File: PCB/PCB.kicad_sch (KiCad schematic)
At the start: 6 parts

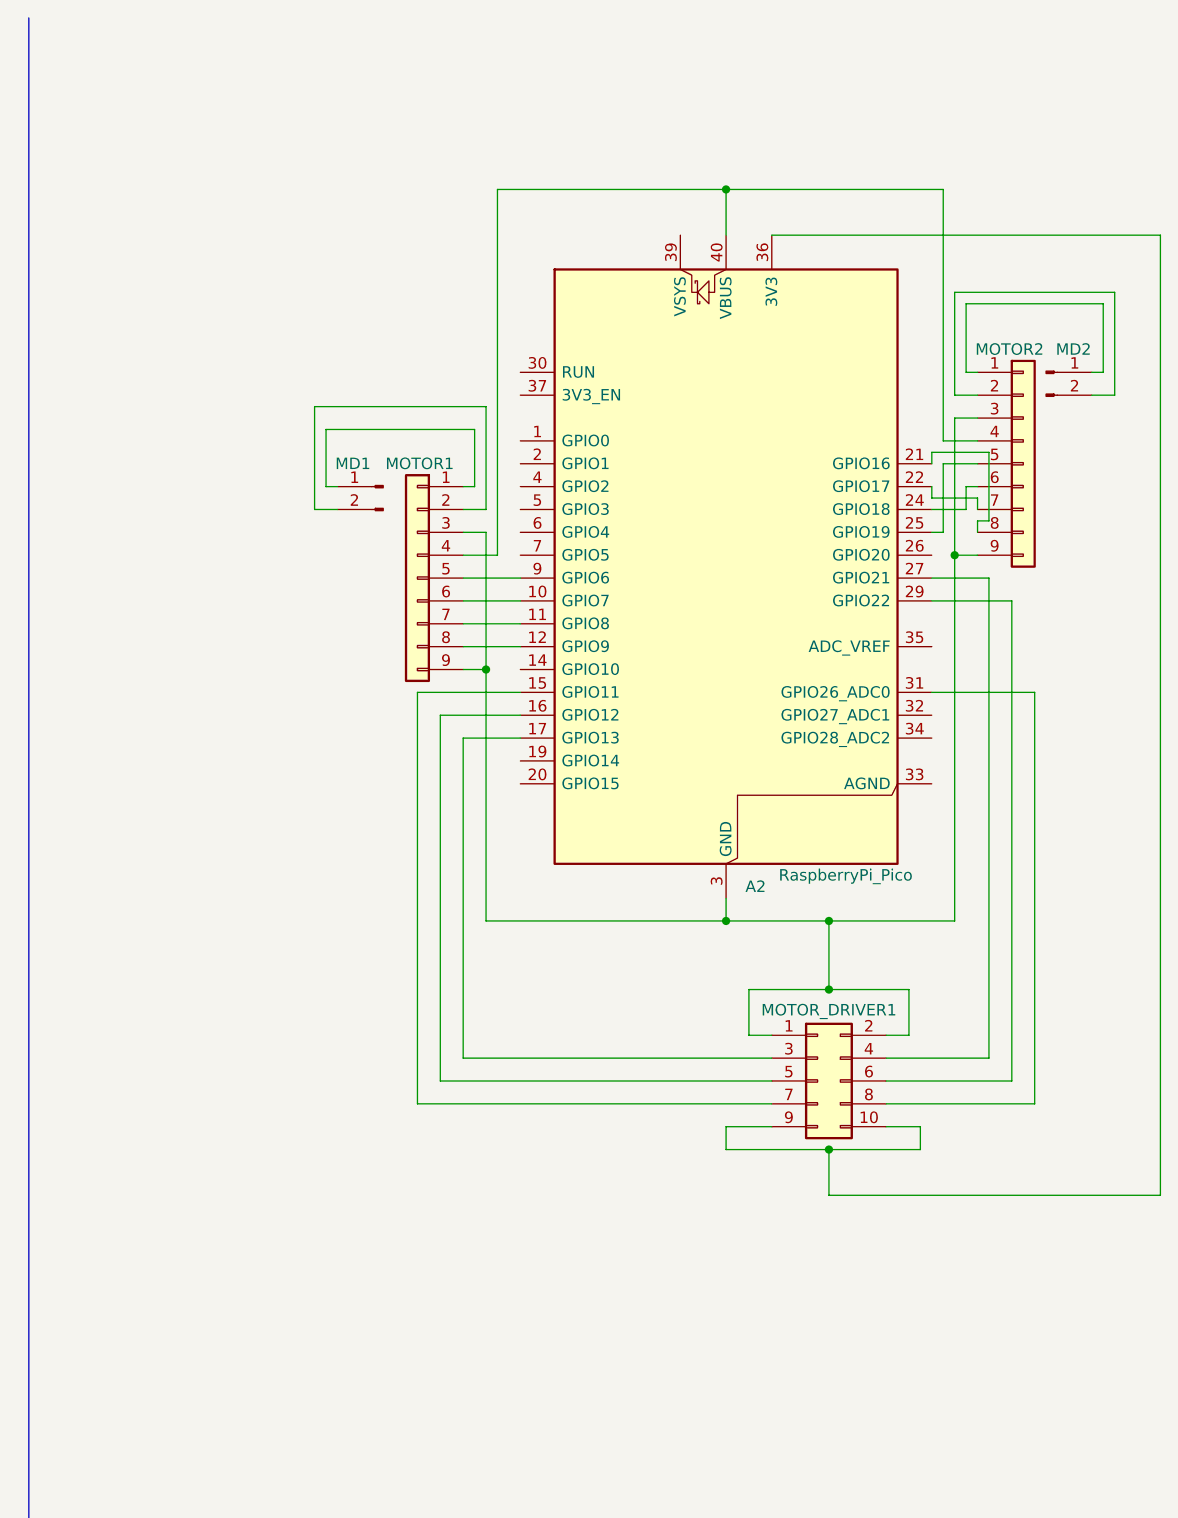
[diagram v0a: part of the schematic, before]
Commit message: update motor driver connection
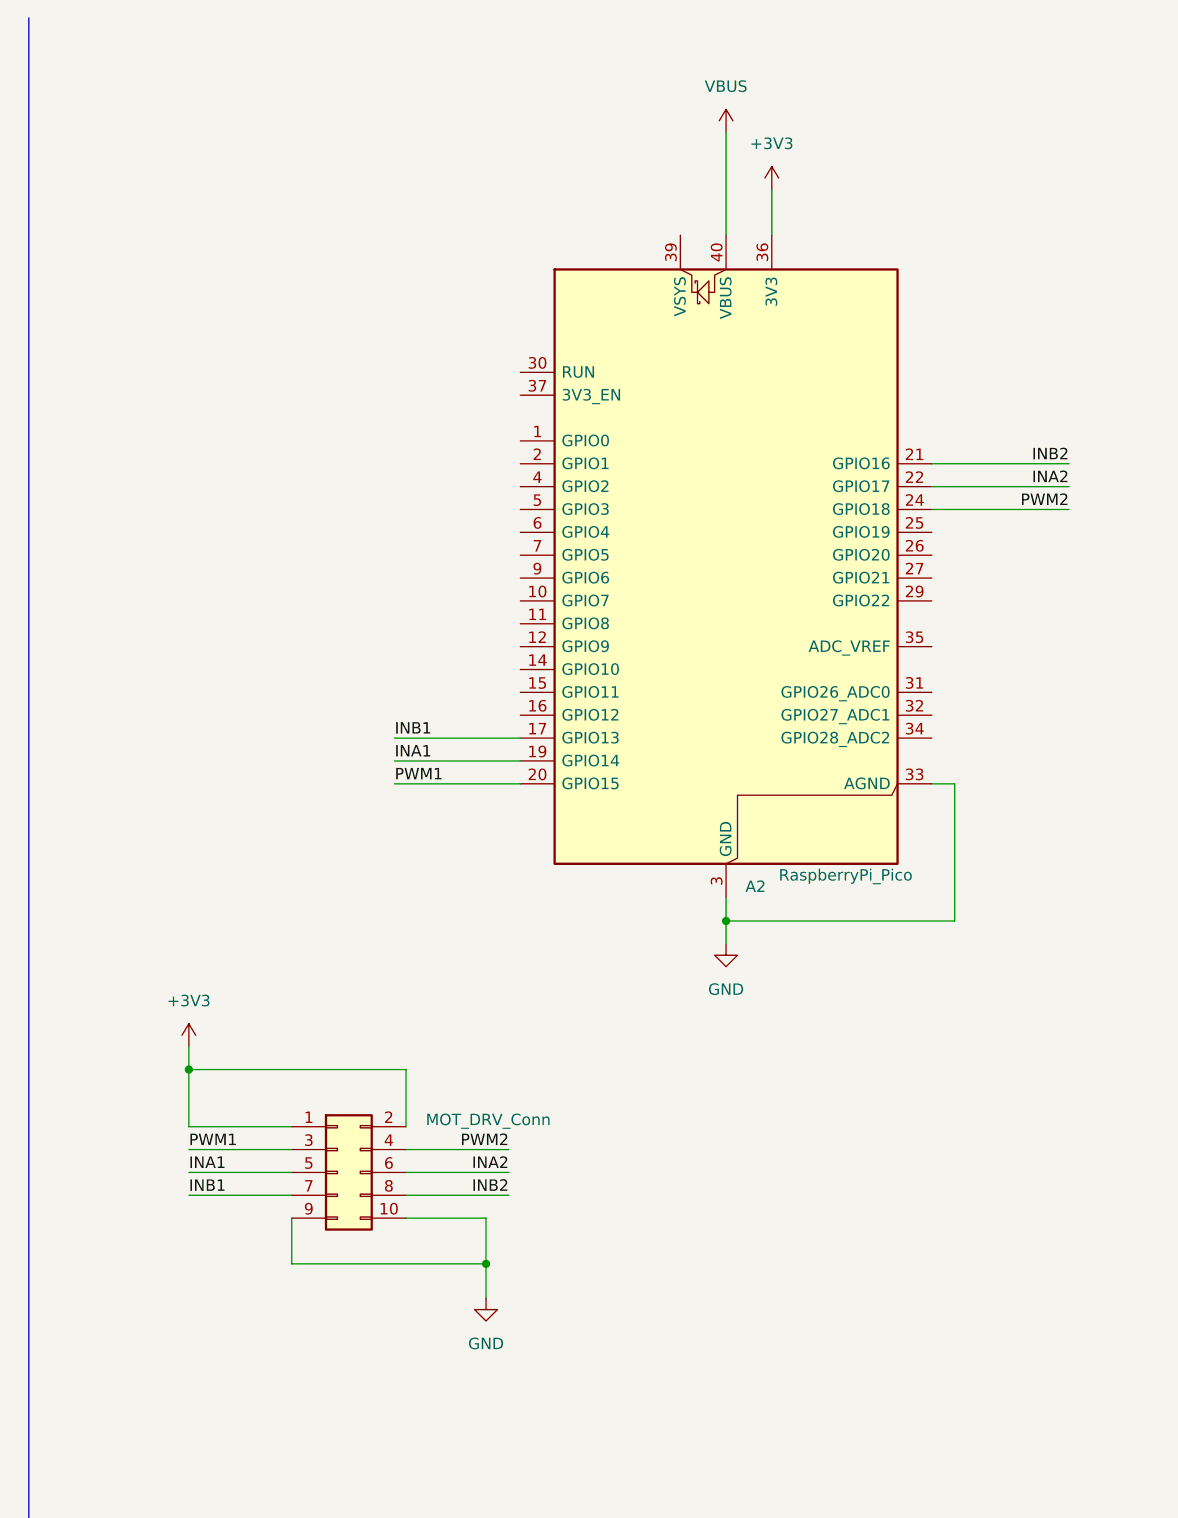
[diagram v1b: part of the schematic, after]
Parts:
- removed MD1, MD2: Conn_01x02_Pin, Connector_PinHeader_2.54mm:PinHeader_1x02_P2.54mm_Vertical, symbol Connector:Conn_01x02_Pin
- removed MOTOR1, MOTOR2: Conn_01x09, Connector_PinHeader_2.54mm:PinHeader_1x09_P2.54mm_Vertical, symbol Connector_Generic:Conn_01x09
- renumbered MOTOR_DRIVER1 to MOT_DRV_Conn
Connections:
- net GND: now reaches A2.13 (GND), A2.18 (GND), A2.23 (GND), A2.28 (GND), A2.3 (GND), A2.38 (GND), A2.8 (GND)
- net GND: now also A2.33 (AGND), MOT_DRV_Conn.10 (Pin_10), MOT_DRV_Conn.9 (Pin_9); no longer MOT_DRV_Conn.1 (Pin_1), MOT_DRV_Conn.2 (Pin_2)
- net VBUS: now reaches A2.40 (VBUS)
- net PWM2: now reaches A2.24 (GPIO18)
- net PWM2: now also MOT_DRV_Conn.4 (Pin_4)
- net INA2: now reaches A2.22 (GPIO17)
- net INA2: now also MOT_DRV_Conn.6 (Pin_6)
- net INB2: now reaches A2.21 (GPIO16)
- net INB2: now also MOT_DRV_Conn.8 (Pin_8)
- net INB1: now reaches A2.17 (GPIO13)
- net INB1: now also MOT_DRV_Conn.7 (Pin_7); no longer MOT_DRV_Conn.3 (Pin_3)
- net at A2.27 (GPIO21): no longer MOT_DRV_Conn.4 (Pin_4)
- net at A2.16 (GPIO12): no longer MOT_DRV_Conn.5 (Pin_5)
- net at A2.29 (GPIO22): no longer MOT_DRV_Conn.6 (Pin_6)
- net at A2.15 (GPIO11): no longer MOT_DRV_Conn.7 (Pin_7)
- net at A2.31 (GPIO26_ADC0): no longer MOT_DRV_Conn.8 (Pin_8)
- net INA1: now reaches A2.19 (GPIO14)
- net INA1: now also MOT_DRV_Conn.5 (Pin_5)
- net PWM1: now reaches A2.20 (GPIO15)
- net PWM1: now also MOT_DRV_Conn.3 (Pin_3)
- new net +3V3: A2.36 (3V3), MOT_DRV_Conn.1 (Pin_1), MOT_DRV_Conn.2 (Pin_2)
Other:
- moved on the sheet: MOT_DRV_Conn

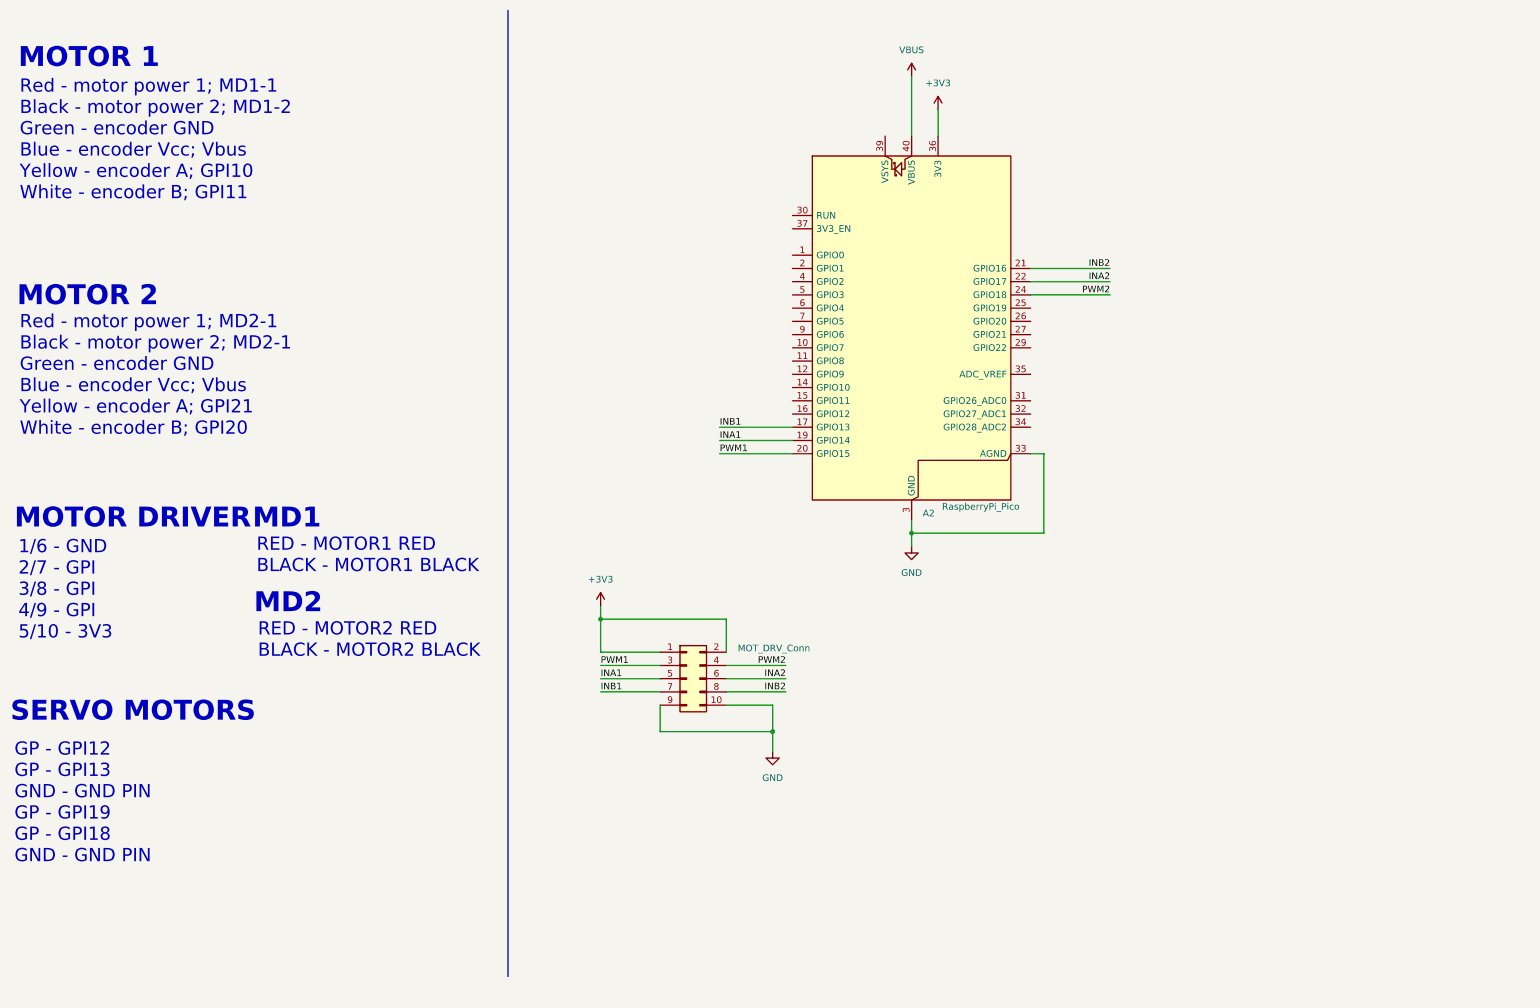
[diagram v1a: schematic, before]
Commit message: update sch with new motor driver connections and servos
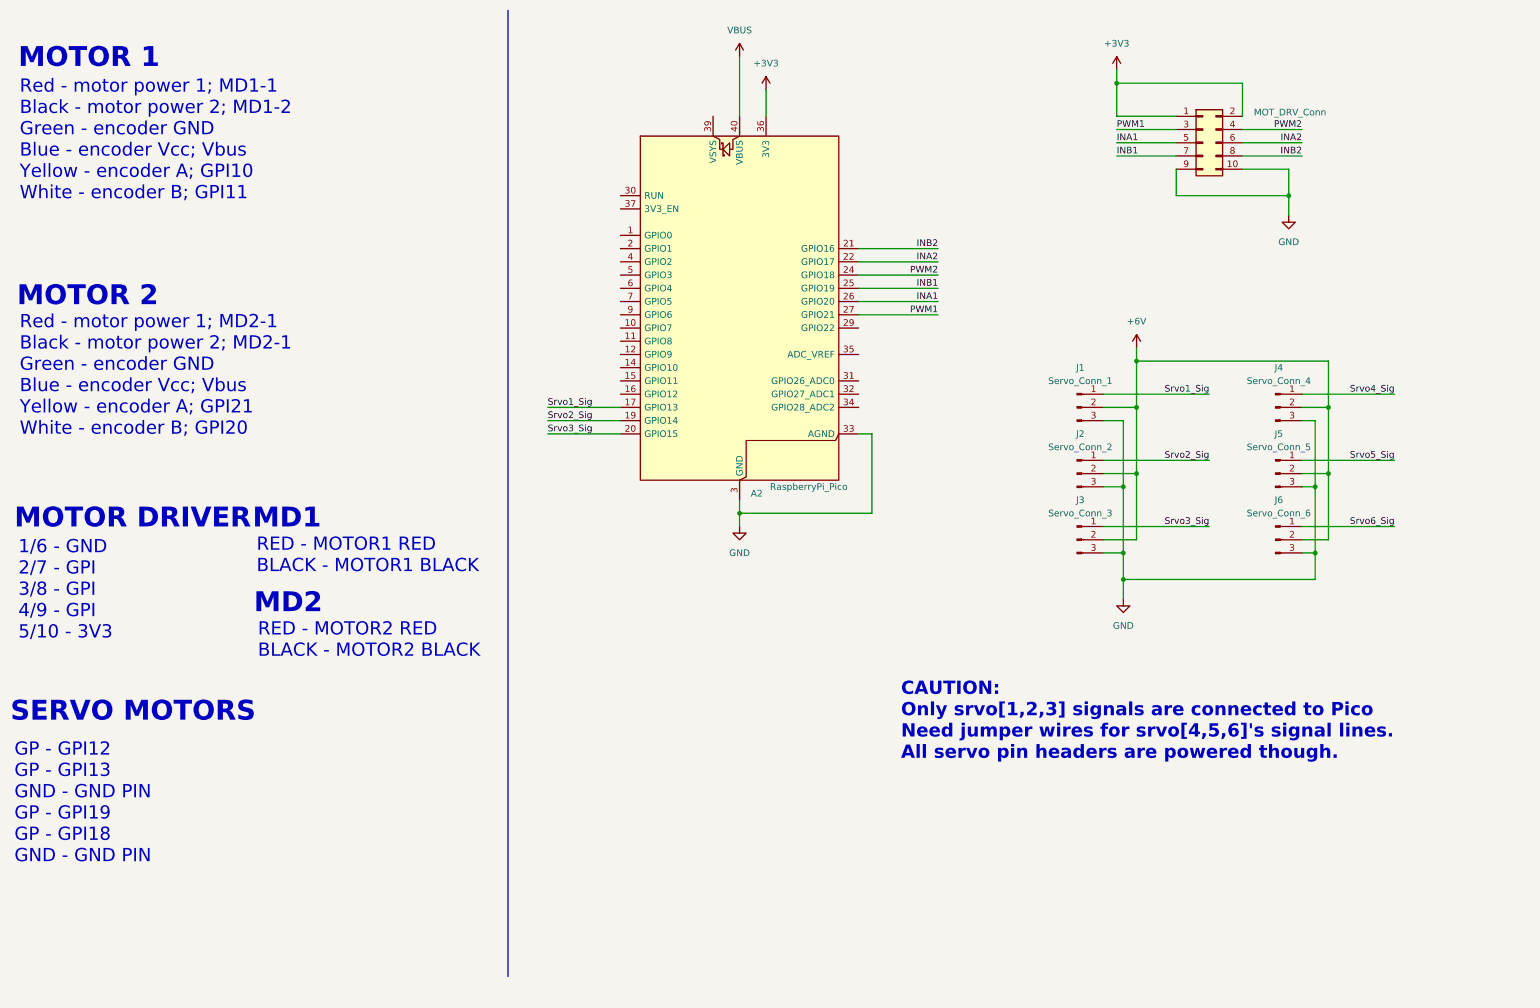
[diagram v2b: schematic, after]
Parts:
- added J1: Servo_Conn_1, symbol Connector:Conn_01x03_Pin
- added J2: Servo_Conn_2, symbol Connector:Conn_01x03_Pin
- added J3: Servo_Conn_3, symbol Connector:Conn_01x03_Pin
- added J4: Servo_Conn_4, symbol Connector:Conn_01x03_Pin
- added J5: Servo_Conn_5, symbol Connector:Conn_01x03_Pin
- added J6: Servo_Conn_6, symbol Connector:Conn_01x03_Pin
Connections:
- net GND: now also J1.3 (Pin_3), J2.3 (Pin_3), J3.3 (Pin_3), J4.3 (Pin_3), J5.3 (Pin_3), J6.3 (Pin_3)
- net INA1: now also A2.26 (GPIO20); no longer A2.19 (GPIO14)
- net INB1: now also A2.25 (GPIO19); no longer A2.17 (GPIO13)
- net PWM1: now also A2.27 (GPIO21); no longer A2.20 (GPIO15)
- new net +6V: J1.2 (Pin_2), J2.2 (Pin_2), J3.2 (Pin_2), J4.2 (Pin_2), J5.2 (Pin_2), J6.2 (Pin_2)
- new net Srvo1_Sig: A2.17 (GPIO13), J1.1 (Pin_1)
- new net Srvo2_Sig: A2.19 (GPIO14), J2.1 (Pin_1)
- new net Srvo3_Sig: A2.20 (GPIO15), J3.1 (Pin_1)
- new net Srvo4_Sig: J4.1 (Pin_1)
- new net Srvo5_Sig: J5.1 (Pin_1)
- new net Srvo6_Sig: J6.1 (Pin_1)
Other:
- note added: "CAUTION: Only srvo[1,2,3] signals are connected to Pico Need jumper wires for srvo[4,5,6]'s signal lines. All servo pin headers are powered though."
- moved on the sheet: A2, MOT_DRV_Conn

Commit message: modify micha's notes
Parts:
- added D1: LED_RKGB, symbol Device:LED_RKGB
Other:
- note removed: "1/6 - GND 2/7 - GPI 3/8 - GPI 4/9 - GPI 5/10 - 3V3"
- note removed: "GP - GPI12 GP - GPI13 GND - GND PIN GP - GPI19 GP - GPI18 GND - GND PIN"
- note removed: "MOTOR DRIVER"
- note removed: "SERVO MOTORS"
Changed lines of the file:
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@@
 	(text "MD1"
 		(exclude_from_sim no)
-		(at 61.468 110.236 0)
+		(at 18.288 96.52 0)
 		(effects
 			(font
 				(face "KiCad Font")
-				(size 3.81 3.81)
+				(size 2.54 2.54)
 				(thickness 0.762)
 				(bold yes)
@@
 	(text "RED - MOTOR1 RED\nBLACK - MOTOR1 BLACK"
 		(exclude_from_sim no)
-		(at 62.23 117.348 0)
+		(at 19.05 103.632 0)
 		(effects
 			(font
 				(face "KiCad Font")
-				(size 2.54 2.54)
+				(size 1.27 1.27)
 			)
 			(justify left)
@@
 	(text "RED - MOTOR2 RED\nBLACK - MOTOR2 BLACK"
 		(exclude_from_sim no)
-		(at 62.484 133.604 0)
+		(at 19.304 119.888 0)
 		(effects
 			(font
 				(face "KiCad Font")
-				(size 2.54 2.54)
+				(size 1.27 1.27)
 			)
 			(justify left)
@@
 			(font
 				(face "KiCad Font")
-				(size 3.81 3.81)
+				(size 2.54 2.54)
 				(thickness 0.762)
 				(bold yes)
@@
 			(font
 				(face "KiCad Font")
-				(size 2.54 2.54)
+				(size 1.27 1.27)
 			)
 			(justify left)
 		)
 	)
-	(text "GP - GPI12\nGP - GPI13\nGND - GND PIN\nGP - GPI19\nGP - GPI18\nGND - GND PIN"
+	(text "MD2"
 		(exclude_from_sim no)
-		(at 15.748 164.846 0)
+		(at 18.542 112.776 0)
 		(effects
 			(font
 				(face "KiCad Font")
 				(size 2.54 2.54)
-			)
-			(justify left)
-		)
-	)
-	(text "SERVO MOTORS"
-		(exclude_from_sim no)
-		(at 14.986 147.32 0)
-		(effects
-			(font
-				(face "KiCad Font")
-				(size 3.81 3.81)
-				(thickness 0.762)
-				(bold yes)
-			)
-			(justify left)
-		)
-	)
-	(text "MD2"
-		(exclude_from_sim no)
-		(at 61.722 126.492 0)
-		(effects
-			(font
-				(face "KiCad Font")
-				(size 3.81 3.81)
-				(thickness 0.762)
-				(bold yes)
-			)
-			(justify left)
-		)
-	)
-	(text "MOTOR DRIVER"
-		(exclude_from_sim no)
-		(at 15.748 110.236 0)
-		(effects
-			(font
-				(face "KiCad Font")
-				(size 3.81 3.81)
 				(thickness 0.762)
 				(bold yes)
@@
 			(font
 				(face "KiCad Font")
-				(size 3.81 3.81)
+				(size 2.54 2.54)
 				(thickness 0.762)
 				(bold yes)
-			)
-			(justify left)
-		)
-	)
-	(text "1/6 - GND\n2/7 - GPI\n3/8 - GPI\n4/9 - GPI\n5/10 - 3V3\n"
-		(exclude_from_sim no)
-		(at 16.51 123.952 0)
-		(effects
-			(font
-				(face "KiCad Font")
-				(size 2.54 2.54)
 			)
 			(justify left)
@@
 			(font
 				(face "KiCad Font")
-				(size 2.54 2.54)
+				(size 1.27 1.27)
 			)
 			(justify left)
@@
 			(width 0)
 			(type default)
-		)
-	)
-	(polyline
-		(pts
-			(xy 110.49 12.7) (xy 110.49 198.12)
-		)
-		(stroke
-			(width 0)
-			(type default)
-			(color 132 0 0 1)
 		)
 	)
@@
 					(unit 1)
 				)
+			)
+		)
+	)
+	(symbol
+		(lib_id "Device:LED_RKGB")
+		(at 135.89 162.56 0)
+		(unit 1)
+		(exclude_from_sim no)
+		(in_bom yes)
+		(on_board yes)
+		(dnp no)
+		(fields_autoplaced yes)
+		(property "Reference" "D1"
+			(at 135.89 148.59 0)
+			(effects
+				(font
+					(size 1.27 1.27)
+				)
+			)
+		)
+		(property "Value" "LED_RKGB"
+			(at 135.89 151.13 0)
+			(effects
+				(font
+					(size 1.27 1.27)
+				)
+			)
+		)
+		(property "Footprint" ""
+			(at 135.89 163.83 0)
+			(effects
+				(font
+					(size 1.27 1.27)
+				)
+				(hide yes)
+			)
+		)
+		(property "Datasheet" "~"
+			(at 135.89 163.83 0)
+			(effects
+				(font
+					(size 1.27 1.27)
+				)
+				(hide yes)
+			)
+		)
+		(property "Description" "RGB LED, red/cathode/green/blue"
+			(at 135.89 162.56 0)
+			(effects
+				(font
+					(size 1.27 1.27)
+				)
+				(hide yes)
+			)
+		)
+		(pin "1"
+		)
+		(pin "4"
+		)
+		(pin "3"
+		)
+		(pin "2"
+		)
+		(instances
+			(project ""
+				(path "/108ca819-7acb-4683-8ce1-30bbf8b45c37"
+					(reference "D1")
+					(unit 1)
+				)
